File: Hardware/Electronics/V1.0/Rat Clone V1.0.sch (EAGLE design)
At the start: 46 parts, among them IC1 LM308, Q1 2N5458

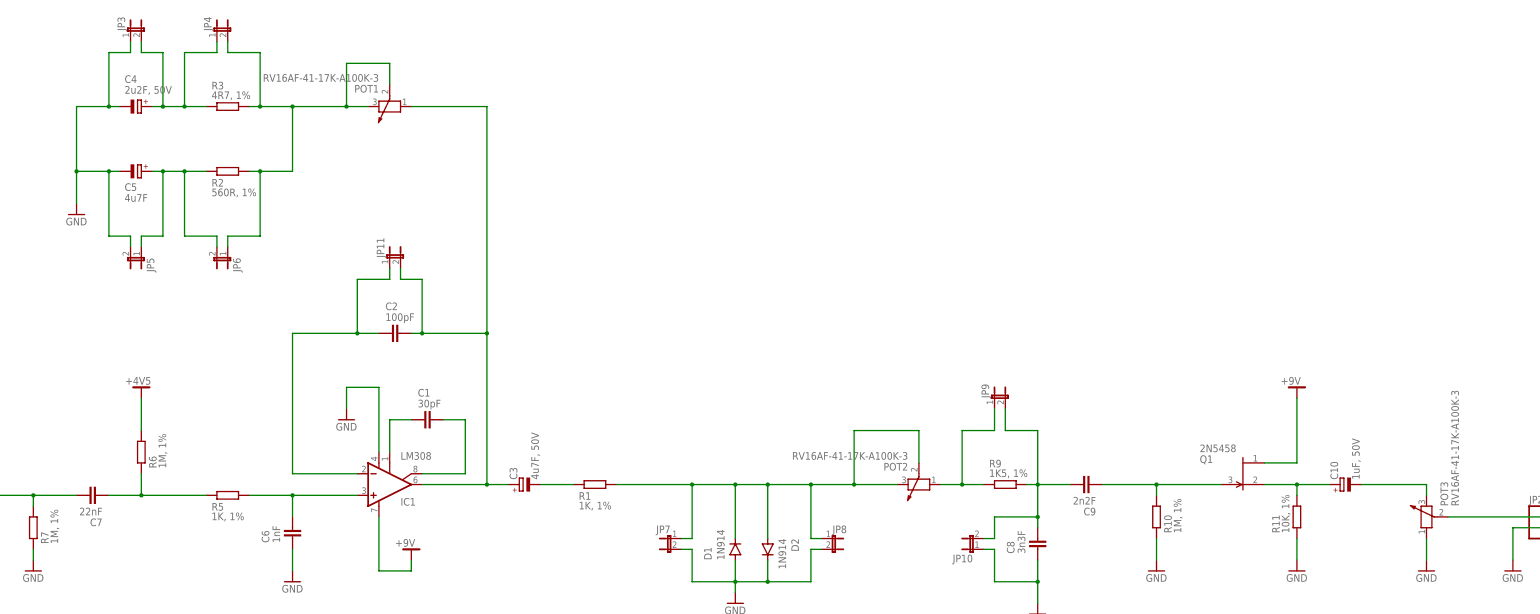
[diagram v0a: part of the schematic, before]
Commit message: Moved to screw mounted PCB
Basic routing
2 layer same price as 1 layer
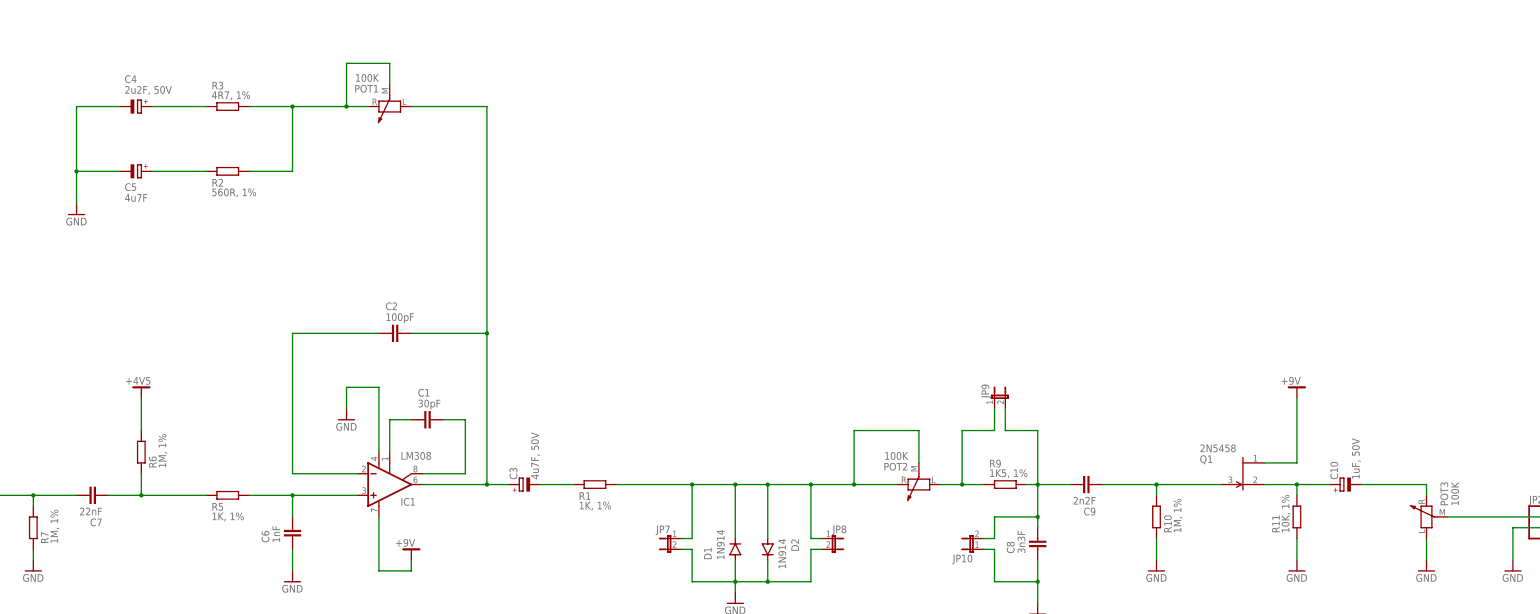
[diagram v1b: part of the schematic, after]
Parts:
- removed JP11, JP3, JP4, JP5, JP6: (no value), jumper:JP1E
- POT1, POT2, POT3: value RV16AF-41-17K-A100K-3 -> 100K; device Custom_Pots:RV16AF-41-17K-A100K-3 -> Custom_Pots:WIRED_POT
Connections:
- net GND: no longer JP3.1, JP5.2
- net N$10: no longer JP5.1, JP6.2
- net N$21: no longer JP3.2, JP4.1
- net N$4: no longer JP11.2
- net N$5: no longer JP11.1
- net N$7: no longer JP4.2, JP6.1
